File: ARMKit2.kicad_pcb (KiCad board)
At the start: 2 copper layers, 44 parts, among them P1 CONN_01X06, P2 CONN_01X32, P3 CONN_01X32, P4 USB_B, SW1 SW_PUSH, SW2 SW_PUSH, U1 STM32F405RG, U2 LT1761, Y1 Crystal, Y2 Crystal

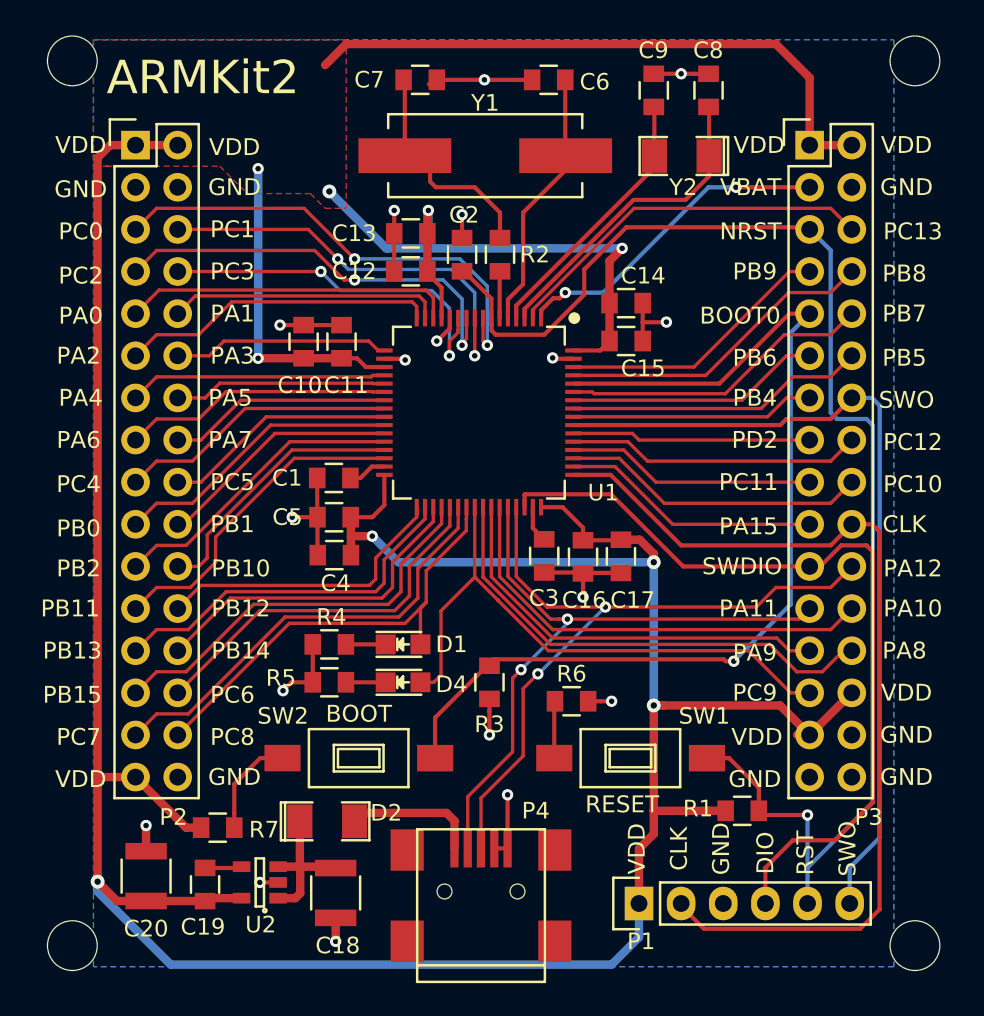
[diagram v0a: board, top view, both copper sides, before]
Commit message: Cleaned up some unused caps, added CC Attribution license
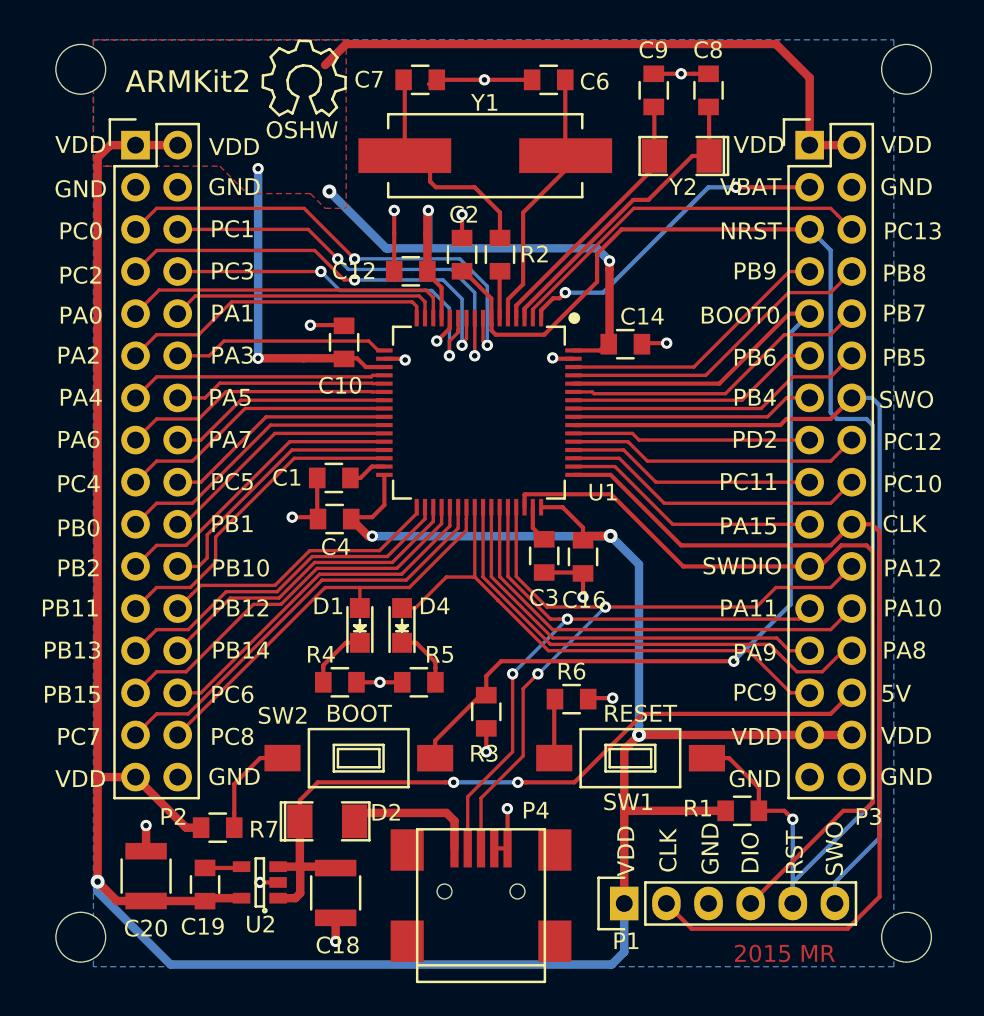
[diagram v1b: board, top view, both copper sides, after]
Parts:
- removed C11, C13, C15, C17, C5: 4.7uF, Capacitors_SMD:C_0805
- removed the REF** at (50.8, 83.8)
- removed the REF** at (101.6, 83.8)
- removed the REF** at (101.6, 137.2)
- removed the REF** at (50.8, 137.2)
- added REF**: Symbol_OSHW-Logo_SilkScreen, Symbols:Symbol_OSHW-Logo_SilkScreen, F.Cu at (64.8, 85.1)
- added REF**: MountingHole_3mm, Mounting_Holes:MountingHole_3mm, F.Cu at (51.3, 84.3)
- added REF**: MountingHole_3mm, Mounting_Holes:MountingHole_3mm, F.Cu at (101.1, 84.3)
- added REF**: MountingHole_3mm, Mounting_Holes:MountingHole_3mm, F.Cu at (101.1, 136.7)
- added REF**: MountingHole_3mm, Mounting_Holes:MountingHole_3mm, F.Cu at (51.3, 136.7)
- moved R5 5.40 mm to (71.7, 121.3)
- moved D4 3.43 mm to (70.7, 117.9), turned to 90 degrees
- moved D1 2.84 mm to (68.1, 117.9), turned to 90 degrees
- moved C14 2.48 mm to (84.1, 100.9)
- moved C10 2.44 mm to (67.2, 100.8)
- moved R4 2.37 mm to (66.9, 121.3), turned to 0 degrees
- moved C4 2.18 mm to (66.6, 111.4)
- moved R3 1.79 mm to (75.8, 123.1)
- moved P1 0.89 mm to (84.1, 134.6)
- moved R6 0.13 mm to (80.9, 122.3)
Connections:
- P3 pad 28: VDD1 -> 5V_IN
- P3 pad 30: GND -> VDD1
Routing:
- net 5V_IN: track 9.31 -> 46.5 mm, vias 0 -> 2
- net GND: track 53.8 -> 42.1 mm
- net VDD1: track 271.0 -> 263.3 mm
- net PC9: track 35.5 -> 32.5 mm
- net PC8: track 27.7 -> 25.2 mm
- net NRST: track 83.7 -> 85.1 mm
- net Net-(D1-Pad1): track 2.40 -> 3.79 mm
- net Net-(D4-Pad1): track 2.40 -> 3.71 mm
- net PB12: track 18.4 -> 17.2 mm
- net PC6: track 22.7 -> 21.7 mm
- net PC7: track 26.9 -> 25.9 mm
- net PB15: track 24.6 -> 23.7 mm
- net PB14: track 20.4 -> 19.5 mm
- net PB13: track 22.3 -> 21.4 mm
- net SWCLK: track 56.9 -> 57.6 mm
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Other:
- board text added: "2015 MR"
- board text added: "5V"
- board text added: "OSHW"

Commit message: More small changes to PCB, Schematic.  Gerber refresh
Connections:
- P3 pad 3: VBAT -> PC13
- P3 pad 6: PC13 -> VBAT
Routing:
- net VDD1: track 263.3 -> 259.6 mm
- net VBAT: track 19.7 -> 22.3 mm, vias 2 -> 0
- net PC13: track 22.8 -> 20.3 mm
- net NRST: track 85.1 -> 83.1 mm
- net GND: track 42.1 -> 41.0 mm

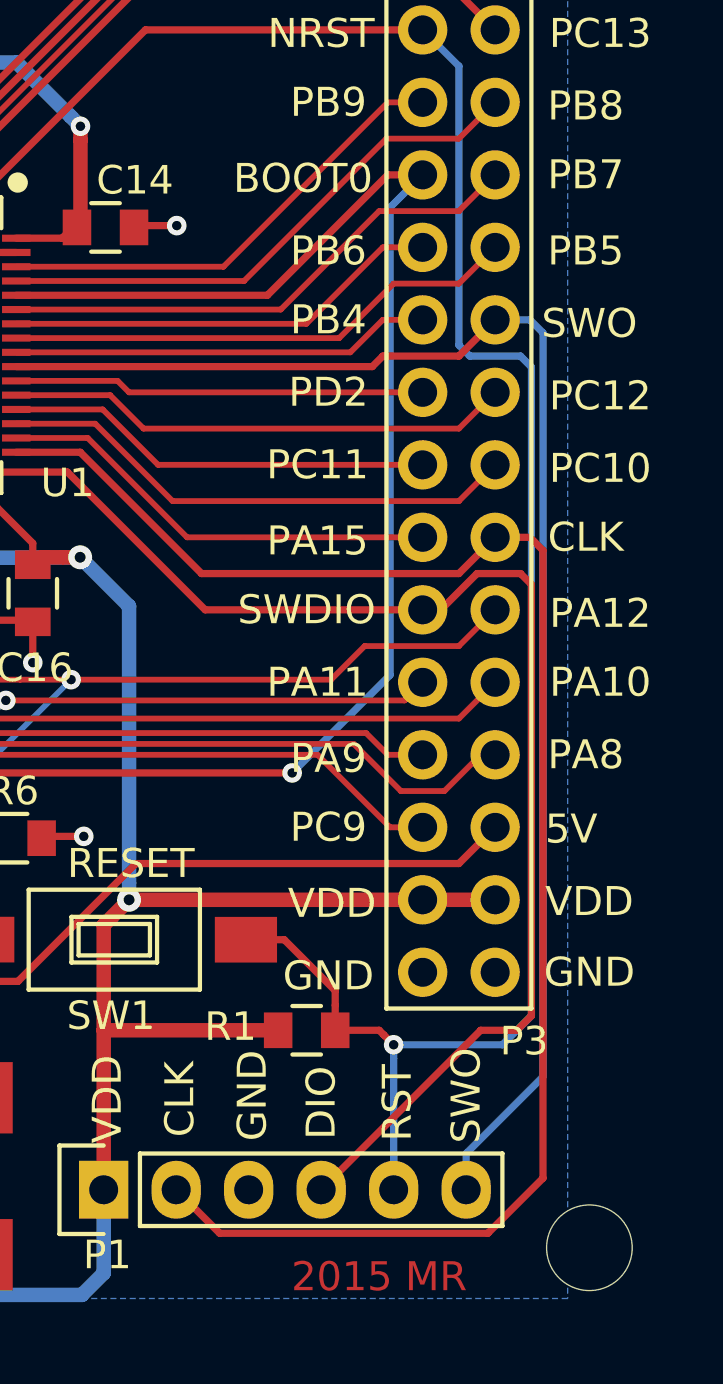
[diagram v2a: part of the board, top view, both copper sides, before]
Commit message: Moved traces that were too close to through-hole headers.  Thanks @_madworm_
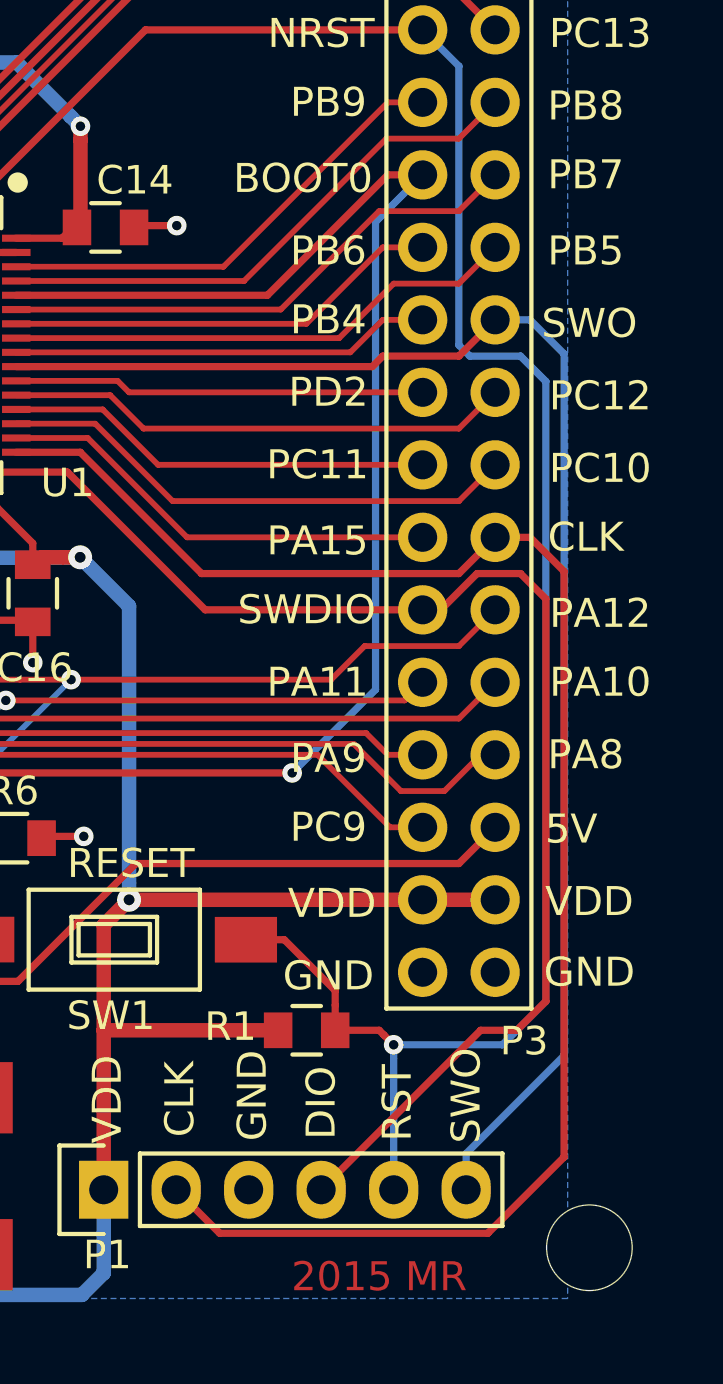
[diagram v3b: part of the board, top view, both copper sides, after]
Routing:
- net SWCLK: track 57.6 -> 58.2 mm
- net TRACESWO: track 51.2 -> 51.8 mm
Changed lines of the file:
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@@
   (segment (start 67.87 108.66) (end 67.564 108.966) (width 0.254) (layer F.Cu) (net 2))
   (segment (start 94.234 129.54) (end 98.044 129.54) (width 0.254) (layer B.Cu) (net 3))
-  (segment (start 99.06 105.791) (end 98.679 105.41) (width 0.254) (layer B.Cu) (net 3))
-  (segment (start 98.044 129.54) (end 99.06 128.524) (width 0.254) (layer B.Cu) (net 3))
-  (segment (start 96.52 95.25) (end 95.25 93.98) (width 0.254) (layer B.Cu) (net 3))
-  (segment (start 99.06 128.524) (end 99.06 105.791) (width 0.254) (layer B.Cu) (net 3))
+  (segment (start 99.568 106.299) (end 98.679 105.41) (width 0.254) (layer B.Cu) (net 3))
+  (segment (start 98.044 129.54) (end 99.568 128.016) (width 0.254) (layer B.Cu) (net 3))
   (segment (start 98.679 105.41) (end 96.901 105.41) (width 0.254) (layer B.Cu) (net 3))
   (segment (start 96.901 105.41) (end 96.52 105.029) (width 0.254) (layer B.Cu) (net 3))
+  (segment (start 99.568 128.016) (end 99.568 106.299) (width 0.254) (layer B.Cu) (net 3))
   (segment (start 96.52 105.029) (end 96.52 95.25) (width 0.254) (layer B.Cu) (net 3))
+  (segment (start 96.52 95.25) (end 95.25 93.98) (width 0.254) (layer B.Cu) (net 3))
   (segment (start 95.25 93.98) (end 85.537922 93.98) (width 0.254) (layer F.Cu) (net 3))
   (segment (start 85.537922 93.98) (end 79.060922 100.457) (width 0.254) (layer F.Cu) (net 3))
@@
   (segment (start 72.6915 120.406) (end 72.6915 121.285) (width 0.254) (layer F.Cu) (net 16))
   (segment (start 97.79 111.76) (end 99.011314 111.76) (width 0.254) (layer F.Cu) (net 17))
-  (segment (start 99.011314 111.76) (end 99.46641 112.215096) (width 0.254) (layer F.Cu) (net 17))
-  (segment (start 99.46641 112.215096) (end 99.46641 134.21359) (width 0.254) (layer F.Cu) (net 17))
-  (segment (start 99.46641 134.21359) (end 97.536 136.144) (width 0.254) (layer F.Cu) (net 17))
   (segment (start 97.536 136.144) (end 88.138 136.144) (width 0.254) (layer F.Cu) (net 17))
+  (segment (start 99.011314 111.76) (end 100.203 112.951686) (width 0.254) (layer F.Cu) (net 17))
+  (segment (start 100.203 112.951686) (end 100.203 133.477) (width 0.254) (layer F.Cu) (net 17))
+  (segment (start 100.203 133.477) (end 97.536 136.144) (width 0.254) (layer F.Cu) (net 17))
   (segment (start 88.138 136.144) (end 86.614 134.62) (width 0.254) (layer F.Cu) (net 17))
   (segment (start 86.614 134.62) (end 86.868 134.874) (width 0.254) (layer F.Cu) (net 17))
@@
   (segment (start 83.252 108.779) (end 87.503 113.03) (width 0.254) (layer F.Cu) (net 17))
   (segment (start 81.011 108.779) (end 83.252 108.779) (width 0.254) (layer F.Cu) (net 17))
+  (segment (start 91.694 134.62) (end 97.282 129.032) (width 0.254) (layer F.Cu) (net 18))
+  (segment (start 97.282 129.032) (end 98.552 129.032) (width 0.254) (layer F.Cu) (net 18))
+  (segment (start 98.552 129.032) (end 99.568 128.016) (width 0.254) (layer F.Cu) (net 18))
+  (segment (start 99.568 128.016) (end 99.568 113.919) (width 0.254) (layer F.Cu) (net 18))
+  (segment (start 99.568 113.919) (end 98.679 113.03) (width 0.254) (layer F.Cu) (net 18))
+  (segment (start 98.679 113.03) (end 97.155 113.03) (width 0.254) (layer F.Cu) (net 18))
+  (segment (start 97.155 113.03) (end 95.885 114.3) (width 0.254) (layer F.Cu) (net 18))
+  (segment (start 95.885 114.3) (end 95.25 114.3) (width 0.254) (layer F.Cu) (net 18))
   (segment (start 78.061 110.729) (end 78.061 109.975) (width 0.254) (layer F.Cu) (net 18))
   (segment (start 78.061 109.975) (end 78.562 109.474) (width 0.254) (layer F.Cu) (net 18))
@@
   (segment (start 78.562 109.474) (end 82.804 109.474) (width 0.254) (layer F.Cu) (net 18))
   (segment (start 82.804 109.474) (end 87.63 114.3) (width 0.254) (layer F.Cu) (net 18))
-  (segment (start 91.694 134.62) (end 97.282 129.032) (width 0.254) (layer F.Cu) (net 18))
-  (segment (start 97.282 129.032) (end 98.552 129.032) (width 0.254) (layer F.Cu) (net 18))
-  (segment (start 98.552 129.032) (end 99.06 128.524) (width 0.254) (layer F.Cu) (net 18))
-  (segment (start 99.06 128.524) (end 99.06 113.411) (width 0.254) (layer F.Cu) (net 18))
-  (segment (start 99.06 113.411) (end 98.679 113.03) (width 0.254) (layer F.Cu) (net 18))
-  (segment (start 98.679 113.03) (end 97.155 113.03) (width 0.254) (layer F.Cu) (net 18))
-  (segment (start 97.155 113.03) (end 95.885 114.3) (width 0.254) (layer F.Cu) (net 18))
-  (segment (start 95.885 114.3) (end 95.25 114.3) (width 0.254) (layer F.Cu) (net 18))
+  (segment (start 97.79 104.14) (end 99.011314 104.14) (width 0.254) (layer B.Cu) (net 19))
+  (segment (start 99.011314 104.14) (end 100.203 105.331686) (width 0.254) (layer B.Cu) (net 19))
+  (segment (start 100.203 105.331686) (end 100.203 129.921) (width 0.254) (layer B.Cu) (net 19))
+  (segment (start 100.203 129.921) (end 96.774 133.35) (width 0.254) (layer B.Cu) (net 19))
   (segment (start 96.774 133.35) (end 96.774 134.62) (width 0.254) (layer B.Cu) (net 19))
-  (segment (start 99.46641 104.595096) (end 99.46641 130.65759) (width 0.254) (layer B.Cu) (net 19))
-  (segment (start 99.46641 130.65759) (end 96.774 133.35) (width 0.254) (layer B.Cu) (net 19))
-  (segment (start 99.011314 104.14) (end 99.46641 104.595096) (width 0.254) (layer B.Cu) (net 19))
-  (segment (start 97.79 104.14) (end 99.011314 104.14) (width 0.254) (layer B.Cu) (net 19))
   (segment (start 97.79 104.14) (end 98.552 104.14) (width 0.254) (layer B.Cu) (net 19))
   (segment (start 97.79 104.14) (end 96.52 105.41) (width 0.254) (layer F.Cu) (net 19))
@@
   (segment (start 93.726 100.33) (end 96.52 100.33) (width 0.2032) (layer F.Cu) (net 22))
   (segment (start 96.52 100.33) (end 97.79 99.06) (width 0.2032) (layer F.Cu) (net 22))
+  (segment (start 95.25 99.06) (end 93.599 100.711) (width 0.254) (layer B.Cu) (net 23))
+  (segment (start 93.599 100.711) (end 93.599 117.094) (width 0.254) (layer B.Cu) (net 23))
+  (segment (start 93.599 117.094) (end 90.678 120.015) (width 0.254) (layer B.Cu) (net 23))
   (segment (start 72.67443 125.85932) (end 72.67443 124.80532) (width 0.254) (layer F.Cu) (net 23))
   (segment (start 72.67443 124.80532) (end 75.41675 122.063) (width 0.254) (layer F.Cu) (net 23))
@@
   (segment (start 89.809686 103.279) (end 81.011 103.279) (width 0.254) (layer F.Cu) (net 23))
   (via (at 90.678 120.015) (size 0.6858) (drill 0.3302) (layers F.Cu B.Cu) (net 23))
-  (segment (start 95.25 99.06) (end 94.106999 100.203001) (width 0.254) (layer B.Cu) (net 23))
-  (segment (start 94.106999 100.203001) (end 94.106999 116.586001) (width 0.254) (layer B.Cu) (net 23))
-  (segment (start 94.106999 116.586001) (end 90.678 120.015) (width 0.254) (layer B.Cu) (net 23))
   (segment (start 97.79 96.52) (end 96.52 97.79) (width 0.2032) (layer F.Cu) (net 24))
   (segment (start 93.98 97.79) (end 88.991 102.779) (width 0.2032) (layer F.Cu) (net 24))
